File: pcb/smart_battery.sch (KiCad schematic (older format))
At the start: 40 parts, among them J1 feather long, J10 feather short, J11 Conn_01x05_RTC, J12 Conn_HtrTh, J13 Conn_BattTh, J2 feather short, J3 feather long, J4 feather short, J5 feather long, J6 feather short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

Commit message: Added connector symbols
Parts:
- J12, J13, JR1, JR2: footprint (none) -> Connector_Molex:Molex_KK-254_AE-6410-02A_1x02_P2.54mm_Vertical
- JM1, JM2: footprint (none) -> Connector_Molex:Molex_KK-254_AE-6410-04A_1x04_P2.54mm_Vertical
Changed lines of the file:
@@
 F 0 "J12" H 1406 2428 50  0000 C CNN
 F 1 "Conn_HtrTh" H 1406 2337 50  0000 C CNN
-F 2 "" H 1300 2250 50  0001 C CNN
+F 2 "Connector_Molex:Molex_KK-254_AE-6410-02A_1x02_P2.54mm_Vertical" H 1300 2250 50  0001 C CNN
 F 3 "~" H 1300 2250 50  0001 C CNN
 	1    1300 2250
@@
 F 0 "J13" H 1973 2230 50  0000 R CNN
 F 1 "Conn_BattTh" H 1973 2321 50  0000 R CNN
-F 2 "" H 2000 2350 50  0001 C CNN
+F 2 "Connector_Molex:Molex_KK-254_AE-6410-02A_1x02_P2.54mm_Vertical" H 2000 2350 50  0001 C CNN
 F 3 "~" H 2000 2350 50  0001 C CNN
 	1    2000 2350
@@
 F 0 "JR2" H 5923 5380 50  0000 R CNN
 F 1 "SolarRelay" H 5923 5471 50  0000 R CNN
-F 2 "" H 5950 5500 50  0001 C CNN
+F 2 "Connector_Molex:Molex_KK-254_AE-6410-02A_1x02_P2.54mm_Vertical" H 5950 5500 50  0001 C CNN
 F 3 "~" H 5950 5500 50  0001 C CNN
 	1    5950 5500
@@
 F 0 "JR1" H 6973 5380 50  0000 R CNN
 F 1 "PowerRelay" H 6973 5471 50  0000 R CNN
-F 2 "" H 7000 5500 50  0001 C CNN
+F 2 "Connector_Molex:Molex_KK-254_AE-6410-02A_1x02_P2.54mm_Vertical" H 7000 5500 50  0001 C CNN
 F 3 "~" H 7000 5500 50  0001 C CNN
 	1    7000 5500
@@
 	4100 6050 4200 6050
 $Comp
-L power:GND #PWR?
+L power:GND #PWR0103
 U 1 1 6024E55B
 P 4200 6500
-F 0 "#PWR?" H 4200 6250 50  0001 C CNN
+F 0 "#PWR0103" H 4200 6250 50  0001 C CNN
 F 1 "GND" H 4205 6327 50  0000 C CNN
 F 2 "" H 4200 6500 50  0001 C CNN
@@
 Connection ~ 4100 5350
 $Comp
-L power:+5V #PWR?
+L power:+5V #PWR0104
 U 1 1 601F6B4D
 P 3250 2450
-F 0 "#PWR?" H 3250 2300 50  0001 C CNN
+F 0 "#PWR0104" H 3250 2300 50  0001 C CNN
 F 1 "+5V" H 3265 2623 50  0000 C CNN
 F 2 "" H 3250 2450 50  0001 C CNN
@@
 	3250 2650 3250 2450
 $Comp
-L power:GND #PWR?
+L power:GND #PWR0105
 U 1 1 602008F6
 P 3300 2750
-F 0 "#PWR?" H 3300 2500 50  0001 C CNN
+F 0 "#PWR0105" H 3300 2500 50  0001 C CNN
 F 1 "GND" H 3305 2577 50  0000 C CNN
 F 2 "" H 3300 2750 50  0001 C CNN
@@
 F 0 "JM1" H 3006 3028 50  0000 C CNN
 F 1 "RockBLOCK Modem" H 3006 2937 50  0000 C CNN
-F 2 "" H 2900 2750 50  0001 C CNN
+F 2 "Connector_Molex:Molex_KK-254_AE-6410-04A_1x04_P2.54mm_Vertical" H 2900 2750 50  0001 C CNN
 F 3 "~" H 2900 2750 50  0001 C CNN
 	1    2900 2750
@@
 F 0 "JM2" H 9156 5428 50  0000 C CNN
 F 1 "I2C Connector" H 9156 5337 50  0000 C CNN
-F 2 "" H 9050 5150 50  0001 C CNN
+F 2 "Connector_Molex:Molex_KK-254_AE-6410-04A_1x04_P2.54mm_Vertical" H 9050 5150 50  0001 C CNN
 F 3 "~" H 9050 5150 50  0001 C CNN
 	1    9050 5150
@@
 $EndComp
 $Comp
-L power:+5V #PWR?
+L power:+5V #PWR0106
 U 1 1 60229670
 P 9500 5000
-F 0 "#PWR?" H 9500 4850 50  0001 C CNN
+F 0 "#PWR0106" H 9500 4850 50  0001 C CNN
 F 1 "+5V" H 9515 5173 50  0000 C CNN
 F 2 "" H 9500 5000 50  0001 C CNN
@@
 	9500 5050 9500 5000
 $Comp
-L power:GND #PWR?
+L power:GND #PWR0107
 U 1 1 60233C1C
 P 9550 5150
-F 0 "#PWR?" H 9550 4900 50  0001 C CNN
+F 0 "#PWR0107" H 9550 4900 50  0001 C CNN
 F 1 "GND" H 9555 4977 50  0000 C CNN
 F 2 "" H 9550 5150 50  0001 C CNN

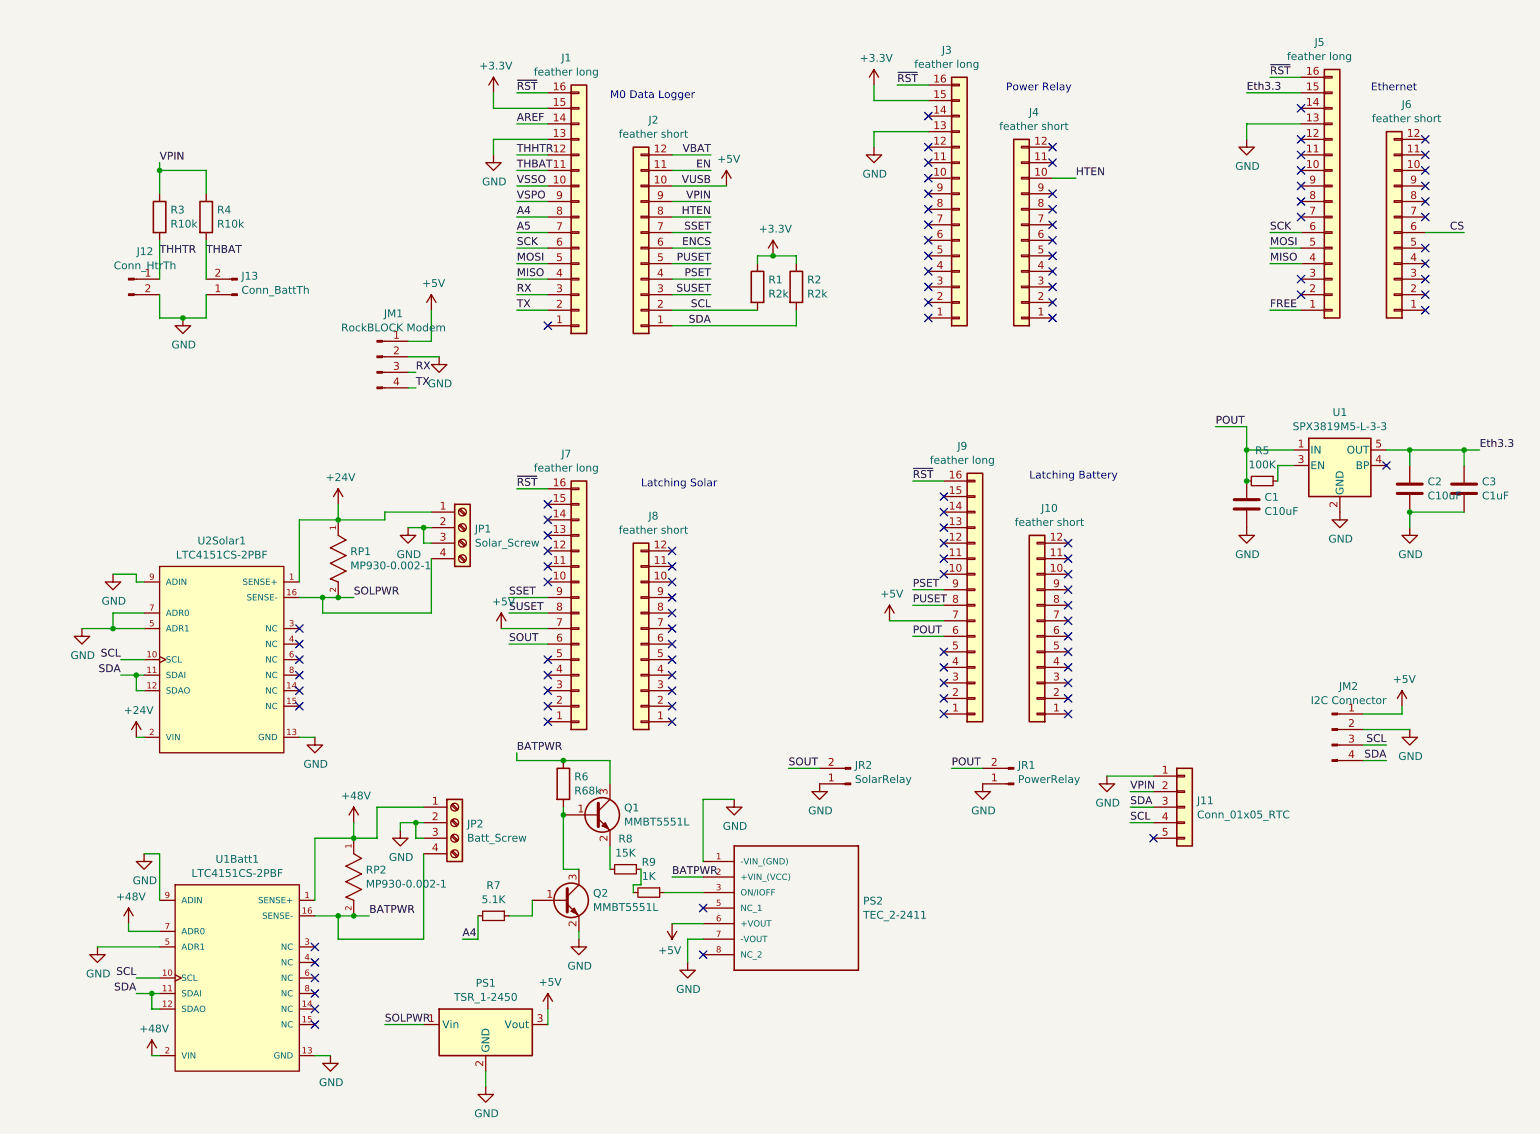
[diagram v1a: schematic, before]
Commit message: Corrected relay pins to match main board
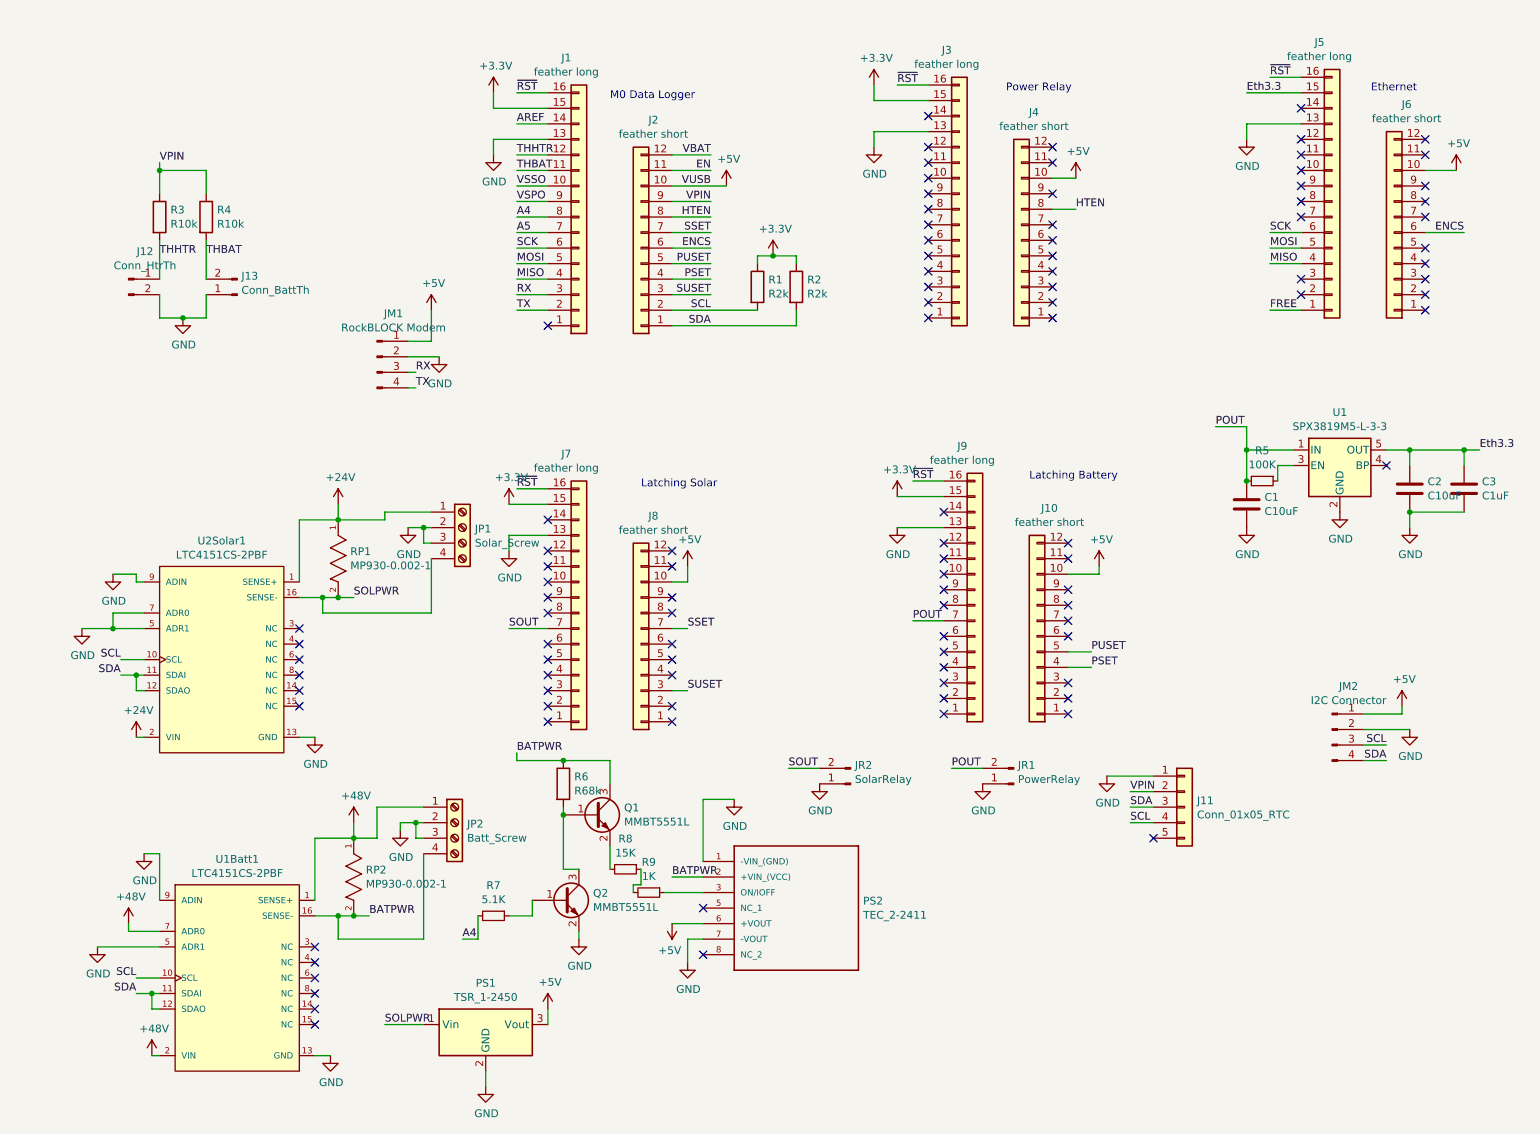
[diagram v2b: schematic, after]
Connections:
- net CS is gone; now on net ENCS: J6.6 (Pin_6)
- net +3V3: now also J7.15 (Pin_15), J9.15 (Pin_15)
- net +5V: now also J10.10 (Pin_10), J4.10 (Pin_10), J6.10 (Pin_10), J8.10 (Pin_10); no longer J7.7 (Pin_7), J9.7 (Pin_7)
- net GND: now also J7.13 (Pin_13), J9.13 (Pin_13)
- net HTEN: now also J4.8 (Pin_8); no longer J4.10 (Pin_10)
- net POUT: now also J9.7 (Pin_7); no longer J9.6 (Pin_6)
- net PSET: now also J10.4 (Pin_4); no longer J9.9 (Pin_9)
- net PUSET: now also J10.5 (Pin_5); no longer J9.8 (Pin_8)
- net SOUT: now also J7.7 (Pin_7); no longer J7.6 (Pin_6)
- net SSET: now also J8.7 (Pin_7); no longer J7.9 (Pin_9)
- net SUSET: now also J8.3 (Pin_3); no longer J7.8 (Pin_8)
- no-connect marks 107 -> 101
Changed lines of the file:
@@
 FREE
 Text Label 9900 1950 2    50   ~ 0
-CS
+ENCS
 Wire Wire Line
 	8650 950  8850 950
@@
 NoConn ~ 9650 1750
 NoConn ~ 9650 1650
-NoConn ~ 9650 1550
 NoConn ~ 9650 1450
 NoConn ~ 9650 1350
@@
 NoConn ~ 7250 2000
 NoConn ~ 7250 1900
-NoConn ~ 7250 1800
 NoConn ~ 7250 1700
 NoConn ~ 7250 1500
@@
 NoConn ~ 4000 4000
 NoConn ~ 4800 4000
-NoConn ~ 4800 4100
-NoConn ~ 4800 4200
 NoConn ~ 4800 4300
 NoConn ~ 4800 4400
-NoConn ~ 4800 4500
 NoConn ~ 4800 4600
 NoConn ~ 4800 4700
@@
 NoConn ~ 6550 4050
 NoConn ~ 6550 4150
-Text Label 6350 4250 0    50   ~ 0
+Text Label 7500 4750 0    50   ~ 0
 PSET
-Wire Wire Line
-	6350 4250 6550 4250
-Text Label 6350 4350 0    50   ~ 0
+Text Label 7500 4650 0    50   ~ 0
 PUSET
-Wire Wire Line
-	6350 4350 6550 4350
 NoConn ~ 6550 4650
 NoConn ~ 6550 4750
@@
 NoConn ~ 7350 4950
 NoConn ~ 7350 4850
-NoConn ~ 7350 4750
-NoConn ~ 7350 4650
 NoConn ~ 7350 4550
 NoConn ~ 7350 4450
 NoConn ~ 7350 4350
 NoConn ~ 7350 4250
-NoConn ~ 7350 4150
 NoConn ~ 7350 4050
 NoConn ~ 7350 3950
@@
 L power:+5V #PWR016
 U 1 1 60141A92
-P 3700 4500
-F 0 "#PWR016" H 3700 4350 50  0001 C CNN
-F 1 "+5V" H 3715 4673 50  0000 C CNN
-F 2 "" H 3700 4500 50  0001 C CNN
-F 3 "" H 3700 4500 50  0001 C CNN
-	1    3700 4500
-	1    0    0    -1
-$EndComp
-Wire Wire Line
-	3700 4500 4000 4500
-Text Label 3750 4600 0    50   ~ 0
+P 4900 4100
+F 0 "#PWR016" H 4900 3950 50  0001 C CNN
+F 1 "+5V" H 4915 4273 50  0000 C CNN
+F 2 "" H 4900 4100 50  0001 C CNN
+F 3 "" H 4900 4100 50  0001 C CNN
+	1    4900 4100
+	1    0    0    -1
+$EndComp
+Text Label 3750 4500 0    50   ~ 0
 SOUT
-Wire Wire Line
-	3750 4600 4000 4600
 $Comp
 L power:+5V #PWR029
 U 1 1 601491D1
-P 6200 4450
-F 0 "#PWR029" H 6200 4300 50  0001 C CNN
-F 1 "+5V" H 6215 4623 50  0000 C CNN
-F 2 "" H 6200 4450 50  0001 C CNN
-F 3 "" H 6200 4450 50  0001 C CNN
-	1    6200 4450
-	1    0    0    -1
-$EndComp
-Wire Wire Line
-	6200 4450 6550 4450
-Text Label 6350 4550 0    50   ~ 0
+P 7550 4100
+F 0 "#PWR029" H 7550 3950 50  0001 C CNN
+F 1 "+5V" H 7565 4273 50  0000 C CNN
+F 2 "" H 7550 4100 50  0001 C CNN
+F 3 "" H 7550 4100 50  0001 C CNN
+	1    7550 4100
+	1    0    0    -1
+$EndComp
+Text Label 6350 4450 0    50   ~ 0
 POUT
-Wire Wire Line
-	6350 4550 6550 4550
 $Comp
 L power:GND #PWR04
@@
 Wire Wire Line
 	1800 2000 1800 2250
-Text Label 7400 1600 0    50   ~ 0
+Text Label 7400 1800 0    50   ~ 0
 HTEN
 Wire Wire Line
@@
 NoConn ~ 6450 1700
 NoConn ~ 6450 1800
-Wire Wire Line
-	3750 4400 4000 4400
-Text Label 3750 4400 0    50   ~ 0
+Text Label 4900 4900 0    50   ~ 0
 SUSET
-Wire Wire Line
-	4000 4300 3750 4300
-Text Label 3750 4300 0    50   ~ 0
+Text Label 4900 4500 0    50   ~ 0
 SSET
 NoConn ~ 4800 4800
-NoConn ~ 4800 4900
 $Comp
 L Connector:Conn_01x02_Male JR2
@@
 Wire Wire Line
 	6600 5400 6800 5400
-NoConn ~ 4000 3900
-NoConn ~ 4000 3700
-NoConn ~ 6550 3850
 NoConn ~ 6550 3750
-NoConn ~ 6550 3650
 $Comp
 L Regulator_Linear:SPX3819M5-L-3-3 U1
@@
 Wire Wire Line
 	5000 5600 5000 6000
+$Comp
+L power:+5V #PWR?
+U 1 1 601FBCB3
+P 7400 1600
+F 0 "#PWR?" H 7400 1450 50  0001 C CNN
+F 1 "+5V" H 7415 1773 50  0000 C CNN
+F 2 "" H 7400 1600 50  0001 C CNN
+F 3 "" H 7400 1600 50  0001 C CNN
+	1    7400 1600
+	1    0    0    -1
+$EndComp
+Wire Wire Line
+	4800 4900 4900 4900
+Wire Wire Line
+	4800 4500 4900 4500
+NoConn ~ 4000 4300
+NoConn ~ 4000 4400
+$Comp
+L power:+3.3V #PWR?
+U 1 1 6023BB19
+P 3750 3700
+F 0 "#PWR?" H 3750 3550 50  0001 C CNN
+F 1 "+3.3V" H 3765 3873 50  0000 C CNN
+F 2 "" H 3750 3700 50  0001 C CNN
+F 3 "" H 3750 3700 50  0001 C CNN
+	1    3750 3700
+	1    0    0    -1
+$EndComp
+Wire Wire Line
+	4000 3700 3750 3700
+NoConn ~ 4800 4100
+Wire Wire Line
+	4800 4200 4900 4200
+Wire Wire Line
+	4900 4200 4900 4100
+NoConn ~ 6550 4250
+NoConn ~ 6550 4350
+Wire Wire Line
+	7350 4650 7500 4650
+Wire Wire Line
+	7350 4750 7500 4750
+$Comp
+L power:+3.3V #PWR?
+U 1 1 60285910
+P 6250 3650
+F 0 "#PWR?" H 6250 3500 50  0001 C CNN
+F 1 "+3.3V" H 6265 3823 50  0000 C CNN
+F 2 "" H 6250 3650 50  0001 C CNN
+F 3 "" H 6250 3650 50  0001 C CNN
+	1    6250 3650
+	1    0    0    -1
+$EndComp
+Wire Wire Line
+	6250 3650 6550 3650
+Wire Wire Line
+	7350 4150 7550 4150
+Wire Wire Line
+	7550 4150 7550 4100
+$Comp
+L power:GND #PWR?
+U 1 1 602A5FC1
+P 6250 3850
+F 0 "#PWR?" H 6250 3600 50  0001 C CNN
+F 1 "GND" H 6255 3677 50  0000 C CNN
+F 2 "" H 6250 3850 50  0001 C CNN
+F 3 "" H 6250 3850 50  0001 C CNN
+	1    6250 3850
+	1    0    0    -1
+$EndComp
+$Comp
+L power:GND #PWR?
+U 1 1 602A601C
+P 3750 4000
+F 0 "#PWR?" H 3750 3750 50  0001 C CNN
+F 1 "GND" H 3755 3827 50  0000 C CNN
+F 2 "" H 3750 4000 50  0001 C CNN
+F 3 "" H 3750 4000 50  0001 C CNN
+	1    3750 4000
+	1    0    0    -1
+$EndComp
+Wire Wire Line
+	4000 3900 3750 3900
+Wire Wire Line
+	3750 3900 3750 4000
+Wire Wire Line
+	6550 3850 6250 3850
+$Comp
+L power:+5V #PWR?
+U 1 1 602BC196
+P 9850 1550
+F 0 "#PWR?" H 9850 1400 50  0001 C CNN
+F 1 "+5V" H 9865 1723 50  0000 C CNN
+F 2 "" H 9850 1550 50  0001 C CNN
+F 3 "" H 9850 1550 50  0001 C CNN
+	1    9850 1550
+	1    0    0    -1
+$EndComp
+Wire Wire Line
+	9650 1550 9850 1550
+Wire Wire Line
+	7250 1800 7400 1800
+Wire Wire Line
+	4000 4500 3750 4500
+NoConn ~ 4000 4600
+Wire Wire Line
+	6550 4450 6350 4450
+NoConn ~ 6550 4550
 $EndSCHEMATC

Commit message: Moving to a feather symbol library
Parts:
- removed J1: feather long, Connector_PinHeader_2.54mm:PinHeader_1x16_P2.54mm_Vertical, symbol Connector_Generic:Conn_01x16
- removed J2: feather short, Connector_PinHeader_2.54mm:PinHeader_1x12_P2.54mm_Vertical, symbol Connector_Generic:Conn_01x12
- removed JR1: PowerRelay, Connector_Molex:Molex_KK-254_AE-6410-02A_1x02_P2.54mm_Vertical, symbol Connector:Conn_01x02_Male
- removed JR2: SolarRelay, Connector_Molex:Molex_KK-254_AE-6410-02A_1x02_P2.54mm_Vertical, symbol Connector:Conn_01x02_Male
- added U10: FEATHER_M0_BASIC_PROTO, SMARTBATT:MODULE_FEATHER_M0_BASIC_PROTO, symbol Adafruit:FEATHER_M0_BASIC_PROTO
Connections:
- net labels removed: SOUT
- wire segments 192 -> 190
- no-connect marks 101 -> 100
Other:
- note removed: "M0 Data Logger"
- moved on the sheet: J12, J13, J3, J4, JM1, R1, R2, R3, R4

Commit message: Moved all feather components to symbols
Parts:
- removed J10, J4, J6, J8: feather short, Connector_PinHeader_2.54mm:PinHeader_1x12_P2.54mm_Vertical, symbol Connector_Generic:Conn_01x12
- removed J3, J5, J7, J9: feather long, Connector_PinHeader_2.54mm:PinHeader_1x16_P2.54mm_Vertical, symbol Connector_Generic:Conn_01x16
- added U11: FEATHERWING_POWER_RELAY, SMARTBATT:MODULE_FEATHER_M0_BASIC_PROTO, symbol Adafruit:FEATHERWING_POWER_RELAY
- added U12: FEATHERWING_ETHERNET, SMARTBATT:MODULE_FEATHER_M0_BASIC_PROTO, symbol Adafruit:FEATHERWING_ETHERNET
- added U13, U14: FEATHERWING_MINI_RELAY, SMARTBATT:MODULE_FEATHER_M0_BASIC_PROTO, symbol Adafruit:FEATHERWING_MINI_RELAY
- U10: value FEATHER_M0_BASIC_PROTO -> FEATHER_M0_ADALOGGER
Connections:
- net labels removed: FREE
- wire segments 190 -> 182
- no-connect marks 100 -> 98
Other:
- note removed: "Ethernet"
- note removed: "Latching Battery"
- note removed: "Latching Solar"
- note removed: "Power Relay"
- moved on the sheet: R1, R2

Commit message: Added footprints for relays and ethernet
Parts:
- U11: footprint SMARTBATT:MODULE_FEATHER_M0_BASIC_PROTO -> SMARTBATT:MODULE_FEATHER_POWER_RELAY
- U12: footprint SMARTBATT:MODULE_FEATHER_M0_BASIC_PROTO -> SMARTBATT:MODULE_FEATHER_ETHERNET_MODULE
- U13, U14: footprint SMARTBATT:MODULE_FEATHER_M0_BASIC_PROTO -> SMARTBATT:MODULE_FEATHER_MINI_RELAY
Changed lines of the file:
@@
 F 0 "U11" H 6250 2967 50  0000 C CNN
 F 1 "FEATHERWING_POWER_RELAY" H 6250 2876 50  0000 C CNN
-F 2 "SMARTBATT:MODULE_FEATHER_M0_BASIC_PROTO" H 5950 2900 50  0001 L BNN
+F 2 "SMARTBATT:MODULE_FEATHER_POWER_RELAY" H 5950 2900 50  0001 L BNN
 F 3 "" H 6800 1750 50  0001 L BNN
 F 4 "Adafruit" H 5950 3100 50  0001 L BNN "MANUFACTURER"
@@
 F 0 "U12" H 9000 3067 50  0000 C CNN
 F 1 "FEATHERWING_ETHERNET" H 9000 2976 50  0000 C CNN
-F 2 "SMARTBATT:MODULE_FEATHER_M0_BASIC_PROTO" H 8700 3000 50  0001 L BNN
+F 2 "SMARTBATT:MODULE_FEATHER_ETHERNET_MODULE" H 8700 3000 50  0001 L BNN
 F 3 "" H 9550 1850 50  0001 L BNN
 F 4 "Adafruit" H 8700 3200 50  0001 L BNN "MANUFACTURER"
@@
 F 0 "U14" H 6750 5317 50  0000 C CNN
 F 1 "FEATHERWING_MINI_RELAY" H 6750 5226 50  0000 C CNN
-F 2 "SMARTBATT:MODULE_FEATHER_M0_BASIC_PROTO" H 6450 5250 50  0001 L BNN
+F 2 "SMARTBATT:MODULE_FEATHER_MINI_RELAY" H 6450 5250 50  0001 L BNN
 F 3 "" H 7300 4100 50  0001 L BNN
 F 4 "Adafruit" H 6450 5450 50  0001 L BNN "MANUFACTURER"
@@
 F 0 "U13" H 4750 5417 50  0000 C CNN
 F 1 "FEATHERWING_MINI_RELAY" H 4750 5326 50  0000 C CNN
-F 2 "SMARTBATT:MODULE_FEATHER_M0_BASIC_PROTO" H 4450 5350 50  0001 L BNN
+F 2 "SMARTBATT:MODULE_FEATHER_MINI_RELAY" H 4450 5350 50  0001 L BNN
 F 3 "" H 5300 4200 50  0001 L BNN
 F 4 "Adafruit" H 4450 5550 50  0001 L BNN "MANUFACTURER"

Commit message: Post review changes
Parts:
- removed JP1: Solar_Screw, symbol Connector:Screw_Terminal_01x04
- removed JP2: Batt_Screw, symbol Connector:Screw_Terminal_01x04
- added JP1: SolarIn, eec:7.5mm_screw_conn_1x2, symbol Connector:Screw_Terminal_01x02
- added JP2: SolarOut, eec:7.5mm_screw_conn_1x3, symbol Connector:Screw_Terminal_01x03
- added JP3: BatteryIn, eec:7.5mm_screw_conn_1x2, symbol Connector:Screw_Terminal_01x02
- added JP4: BatteryOut, eec:7.5mm_screw_conn_1x3, symbol Connector:Screw_Terminal_01x03
- JM1: footprint Connector_Molex:Molex_KK-254_AE-6410-04A_1x04_P2.54mm_Vertical -> Connector_Molex:Molex_KK-254_AE-6410-06A_1x06_P2.54mm_Vertical; symbol Connector:Conn_01x04_Male -> Connector:Conn_01x06_Male
- U11: value FEATHERWING_POWER_RELAY -> FEATHERWING_HEATER_RELAY
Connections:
- net +24V: now also JP1.1 (Pin_1)
- net +3V3: now also U10.P1_15 (3V3), U11.P1_15 (3V3), U13.P1_15 (3V3), U14.P1_15 (3V3); no longer U10.P2_1 (VBAT), U11.P2_1 (VBAT), U13.P2_1 (VBAT), U14.P2_1 (VBAT)
- net +48V: now also JP3.1 (Pin_1)
- net +5V: no longer U12.P2_3 (VBUS)
- net BATPWR: now also JP4.1 (Pin_1)
- net Eth3.3: now also U12.P1_15 (3V3); no longer U12.P2_1 (VBAT)
- net GND: now also JP1.2 (Pin_2), JP2.2 (Pin_2), JP2.3 (Pin_3), JP3.2 (Pin_2), JP4.2 (Pin_2), JP4.3 (Pin_3)
- net RX: no longer JM1.3 (Pin_3)
- net SOLPWR: now also JP2.1 (Pin_1)
- net TX: no longer JM1.4 (Pin_4)
- net VBAT: now also U10.P2_1 (VBAT); no longer U10.P2_2 (EN)
- net ~RST: now also U10.P1_16 (~RESET), U11.P1_16 (~RESET), U12.P1_16 (~RESET), U13.P1_16 (~RESET), U14.P1_16 (~RESET); no longer U10.P1_15 (3V3), U11.P1_15 (3V3), U12.P1_15 (3V3), U13.P1_15 (3V3), U14.P1_15 (3V3)
- net A4 renamed 48VEN
- net A5 renamed RBEN
- net RBEN: now also JM1.6 (Pin_6)
- net VSPO renamed RBTX
- net RBTX: now also JM1.4 (Pin_4)
- net VSSO renamed RBRX
- net RBRX: now also JM1.3 (Pin_3)
- no-connect marks 98 -> 101
